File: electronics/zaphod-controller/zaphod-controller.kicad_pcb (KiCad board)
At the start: 4 copper layers, 199.9 x 69.3 mm, 220 parts, among them P1 MOLEX_43160-0102, P10 CONN_01X01, P11 MOLEX_MINIFIT_JR_2x4_WAY, P12 MOLEX_MINIFIT_JR_2x4_WAY, P13 MOLEX_MINIFIT_JR_2x4_WAY, P14 MOLEX_MINIFIT_JR_2x4_WAY, P17 CONN_01X02, P18 CONN_01X02, P19 CONN_01X02, P2 MOLEX_MINIFIT_JR_2x2_WAY, P20 CONN_01X06, P22 CONN_01X02, P23 MOLEX_KK2.54_1x4_WAY_FAN, P3 MOLEX_MINIFIT_JR_2x2_WAY, P4 MOLEX_MINIFIT_JR_2x2_WAY, P5 MOLEX_MINIFIT_JR_2x2_WAY, Q1 Si7852DP, Q2 Si7852DP, Q3 2N7002P, Q4 NTR1P02T1G, Q5 BC847B, Q6 2N7002P, SW1 B3U-1000P_SPST-NO_SMD, SW2 B3U-1000P_SPST-NO_SMD, SW3 B3U-1000P_SPST-NO_SMD, U1 ISL85410FRZ, U10 ULN2003A, U11 ULN2003A, U2 LM5116, U3 ISL85410FRZ, U4 STM32F429VET6, U5 USBLC6, U6 ACS711KEXLT_15AB, U7 ACS711KEXLT_15AB, U8 ACS711KEXLT_15AB, U9 ACS711KEXLT_15AB, X1 CSTCE8M00G55Z, X2 SWD_SMT_SOCKET, X3 ABS06-107-32.768KHZ

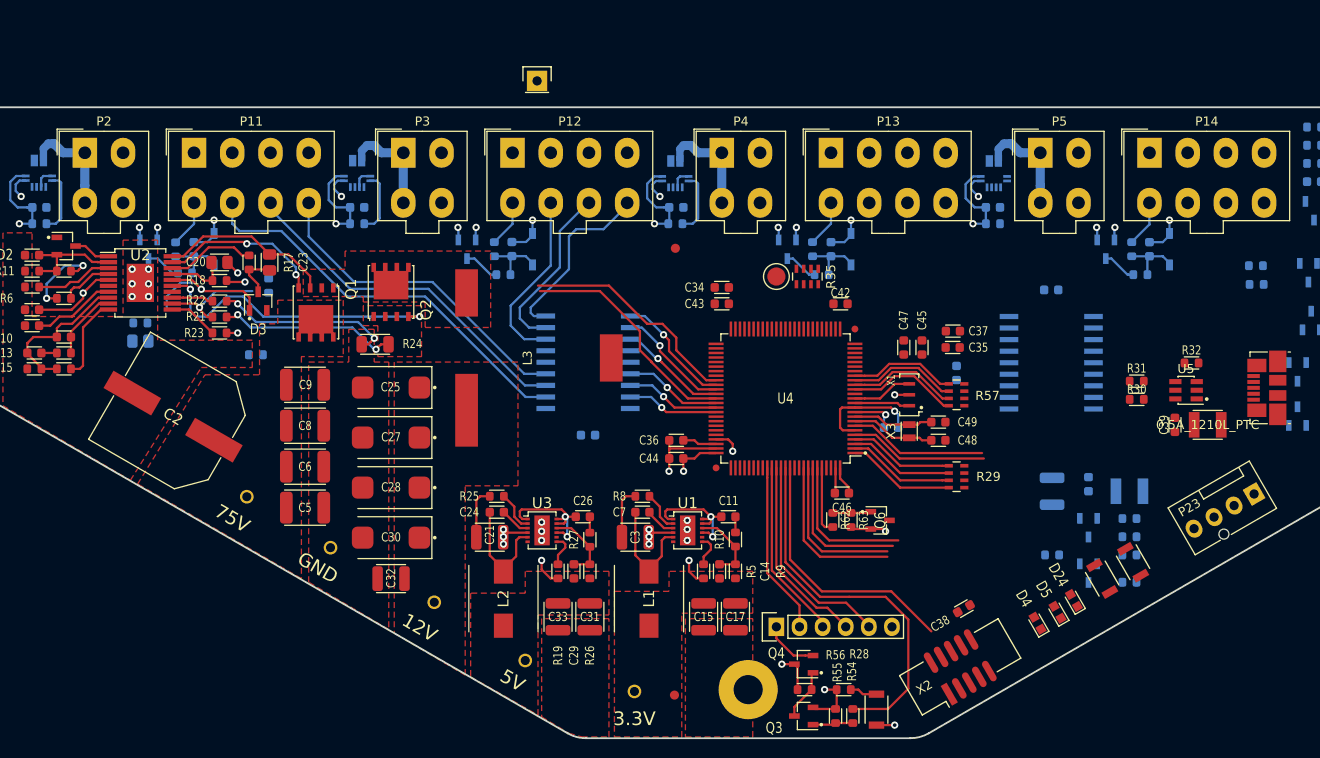
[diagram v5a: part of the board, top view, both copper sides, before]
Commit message: Continued routing and tweaks.
Updated inductor position, repinned ADC for nicer routing, most micro lines fanned out, added logo
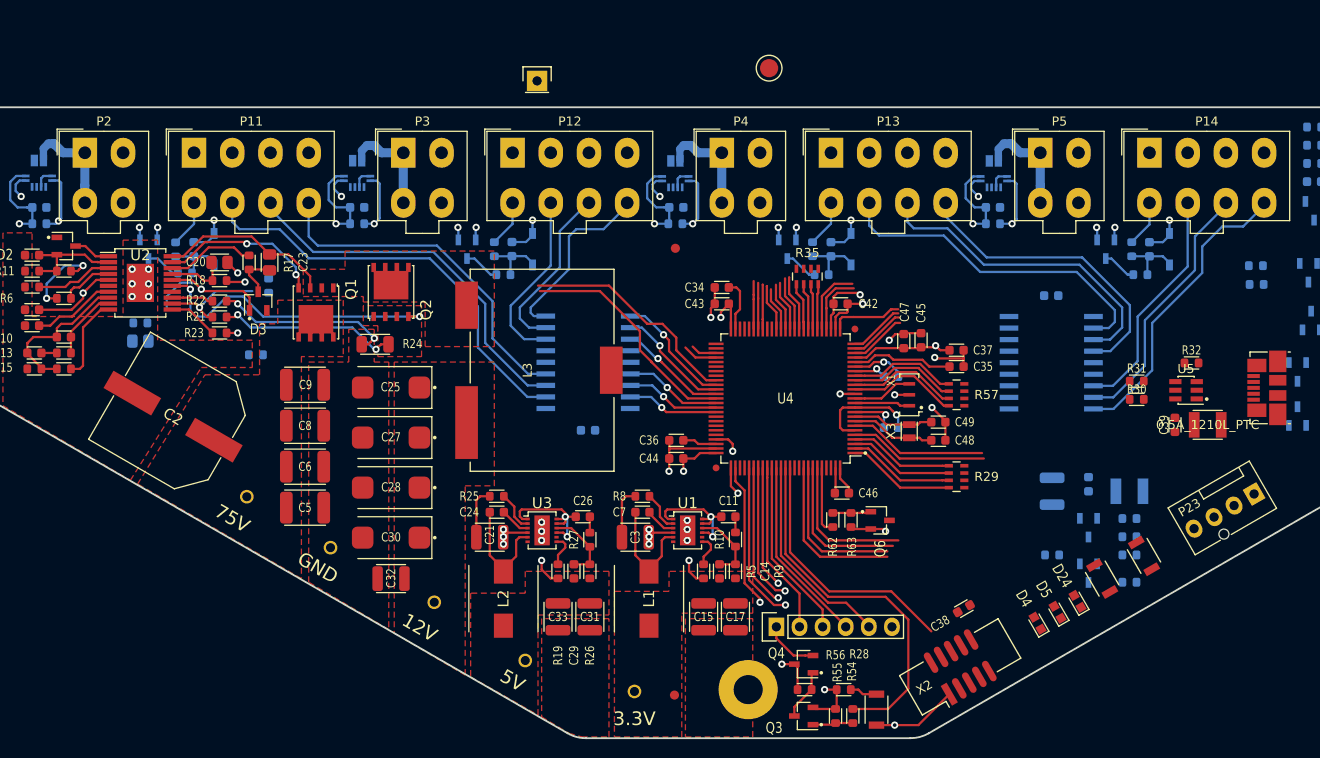
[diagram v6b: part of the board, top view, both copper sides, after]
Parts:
- added G***: LOGO, Applidyne_Logo:PANIC_LOGO890X810, F.Cu at (181.6, 98.5)
- moved TEST8 22.9 mm to (160.2, 45.7)
- moved C41 7.21 mm to (173.6, 79.6), turned to 0 degrees
- moved C35 2.14 mm to (180.8, 78.5)
- moved C37 2.14 mm to (180.8, 76.7)
- moved SW2 1.39 mm to (201.4, 99.3)
- moved L3 1.35 mm to (133.7, 78.9)
- moved C45 0.81 mm to (176.9, 75.6), turned to 90 degrees
- moved C47 0.70 mm to (175.0, 75.7), turned to 90 degrees
- moved C55 0.63 mm to (191.2, 70.7)
- moved C54 0.53 mm to (140.3, 85.5)
- moved D24 0.41 mm to (194.1, 104.3)
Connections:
- R35 pad 5: MOTOR_4_CURRENT -> MOTOR_1_CURRENT
- R35 pad 6: MOTOR_3_CURRENT -> MOTOR_2_CURRENT
- R35 pad 7: MOTOR_2_CURRENT -> MOTOR_3_CURRENT
- R35 pad 8: MOTOR_1_CURRENT -> MOTOR_4_CURRENT
- U4 pad 31: MOTOR_3_CURRENT -> MOTOR_4_CURRENT
- U4 pad 32: MOTOR_4_CURRENT -> MOTOR_3_CURRENT
- U4 pad 33: MOTOR_1_CURRENT -> MOTOR_2_CURRENT
- U4 pad 34: MOTOR_2_CURRENT -> MOTOR_1_CURRENT
- U4 pad 38: ~MOTOR_1_OC -> ~MOTOR_2_OC
- U4 pad 39: ~MOTOR_2_OC -> ~MOTOR_1_OC
- U6 pad 11: Net-(R35-Pad1) -> Net-(R35-Pad4)
- U7 pad 11: Net-(R35-Pad2) -> Net-(R35-Pad3)
- U8 pad 11: Net-(R35-Pad3) -> Net-(R35-Pad2)
- U9 pad 11: Net-(R35-Pad4) -> Net-(R35-Pad1)
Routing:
- net +3.3V: track 71.5 -> 116.4 mm, vias 12 -> 16
- net Net-(P13-Pad6): track 0.00 -> 37.3 mm
- net Net-(P13-Pad7): track 0.00 -> 35.5 mm
- net Net-(P13-Pad8): track 0.00 -> 33.6 mm
- net Net-(P14-Pad8): track 0.00 -> 33.1 mm
- net GND: track 94.6 -> 124.8 mm, vias 29 -> 35
- net Net-(P14-Pad7): track 0.00 -> 28.7 mm
- net Net-(P14-Pad6): track 0.00 -> 25.7 mm
- net EXT_OUTPUT_0: track 0.00 -> 17.5 mm, vias 0 -> 1
- net AUX_PWM_0: track 0.00 -> 15.9 mm, vias 0 -> 1
- net EXT_INPUT_1: track 0.00 -> 15.6 mm, vias 0 -> 1
- net EXT_OUTPUT_1: track 0.00 -> 15.4 mm, vias 0 -> 1
- net EXT_INPUT_0: track 0.00 -> 13.4 mm, vias 0 -> 1
- net ~MOTOR_4_OC: track 0.00 -> 13.2 mm, vias 0 -> 1
- net SERVO4_B: track 0.00 -> 7.93 mm
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
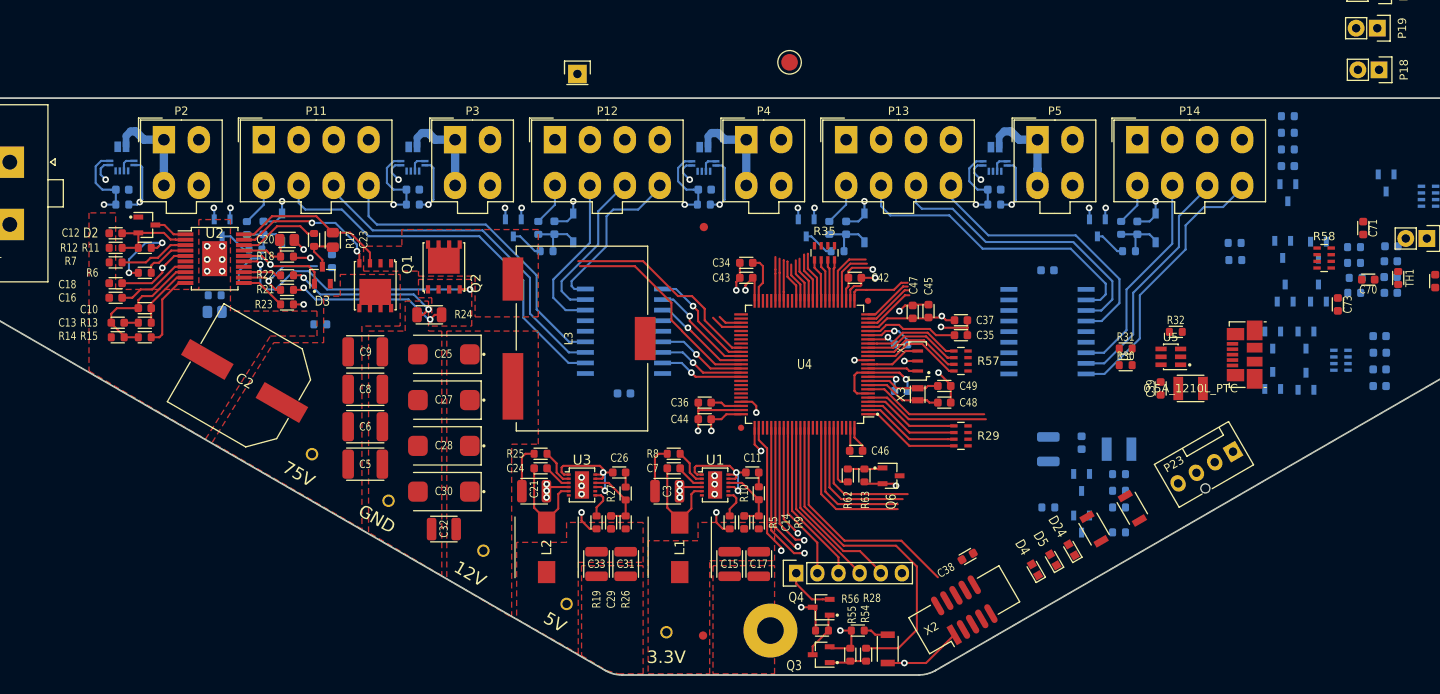
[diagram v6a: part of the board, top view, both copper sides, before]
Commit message: Minor repinning, routing, updated connector metadata
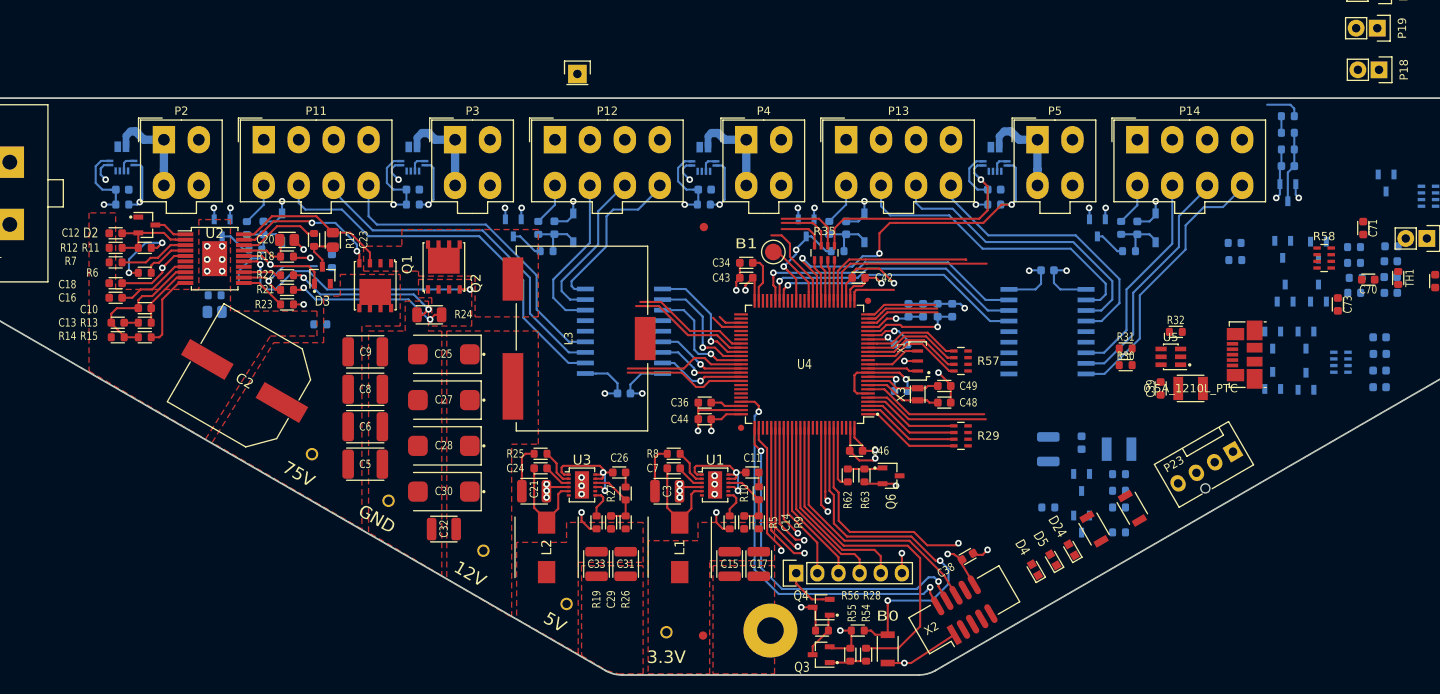
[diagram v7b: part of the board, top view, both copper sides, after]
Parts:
- removed G***: LOGO, Applidyne_Logo:PANIC_LOGO890X810
- C35, C37, C45, C47: moved to B.Cu
- moved TEST8 22.9 mm to (158.2, 68.5)
- moved C35 4.10 mm to (178.0, 75.5), turned to 90 degrees
- moved C45 2.40 mm to (174.5, 75.5)
- moved C37 1.59 mm to (179.8, 75.5), turned to 90 degrees
- moved C47 1.27 mm to (176.2, 75.5)
- moved C42 0.45 mm to (168.5, 71.6)
- moved R48 0.24 mm to (226.5, 81.8)
- moved C60 0.14 mm to (231.1, 78.8)
- moved C61 0.14 mm to (231.1, 80.8)
- moved C62 0.14 mm to (231.1, 82.8)
- moved C63 0.14 mm to (231.1, 84.8)
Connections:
- U4 pad 38: ~MOTOR_2_OC -> Net-(U4-Pad38)
- U4 pad 39: ~MOTOR_1_OC -> Net-(U4-Pad39)
- U4 pad 58: Net-(U4-Pad58) -> ~MOTOR_2_OC
- U4 pad 67: Net-(U4-Pad67) -> ~MOTOR_1_OC
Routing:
- net SWDIO: track 2.84 -> 47.4 mm, vias 1 -> 2
- net SWCLK: track 3.10 -> 42.9 mm, vias 1 -> 2
- net ~MOTOR_4_OC: track 13.2 -> 43.0 mm, vias 1 -> 3
- net SERVO3_B: track 5.27 -> 34.2 mm, vias 0 -> 1
- net SERVO3_A: track 5.07 -> 32.6 mm, vias 0 -> 1
- net GND: track 124.8 -> 152.1 mm, vias 35 -> 40
- net SERVO3_EN: track 4.87 -> 31.5 mm, vias 0 -> 1
- net Net-(R35-Pad1): track 2.86 -> 28.3 mm
- net BOOT0: track 19.6 -> 44.8 mm, vias 0 -> 2
- net AUX_ANALOG_0: track 6.89 -> 21.3 mm
- net +12V: track 23.5 -> 37.8 mm, vias 9 -> 11
- net AUX_ANALOG_1: track 7.52 -> 19.6 mm
- net SERVO1_HLFB: track 29.4 -> 18.3 mm
- net FAN_PWM: track 16.1 -> 27.1 mm, vias 0 -> 1
- net SERVO2_HLFB: track 28.6 -> 18.7 mm
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- added copper zone on In2.Cu, net +3.3V
- added copper zone on In1.Cu, net GND
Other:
- board text added: "B0"
- board text added: "B1"

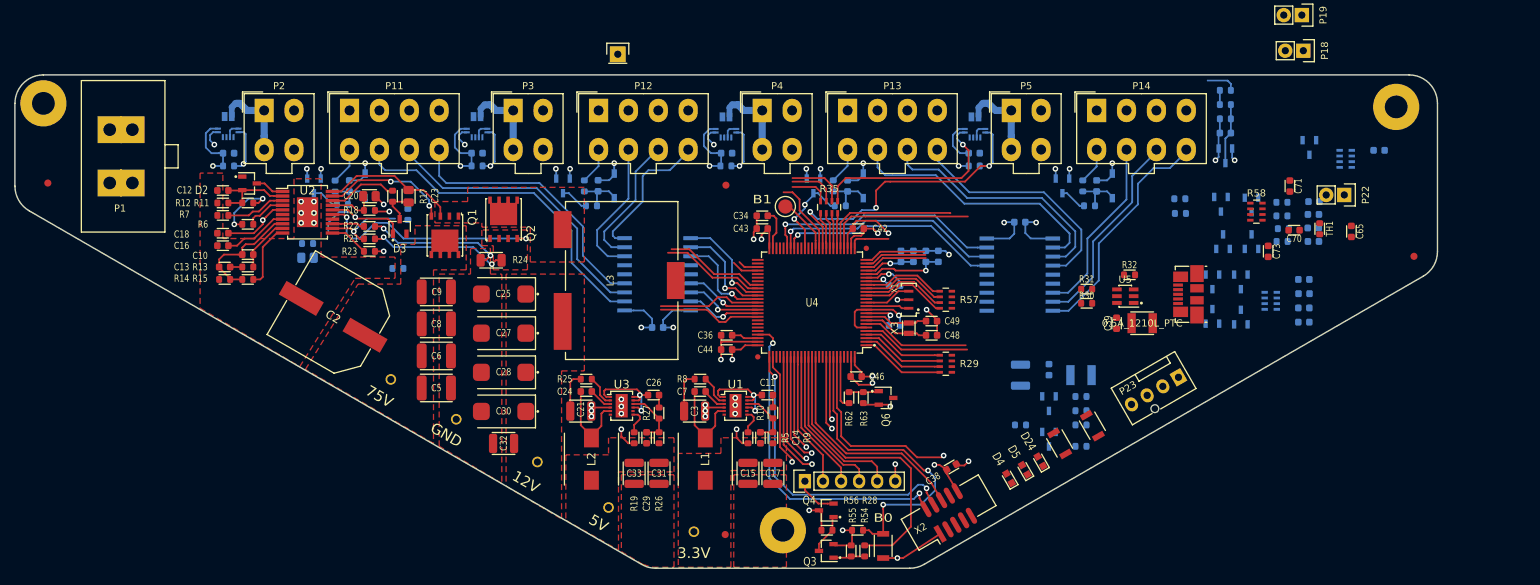
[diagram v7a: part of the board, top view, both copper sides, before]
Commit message: Routing, connector changes, repinning/resistor changes
Misc other cleanup and improvements while routing
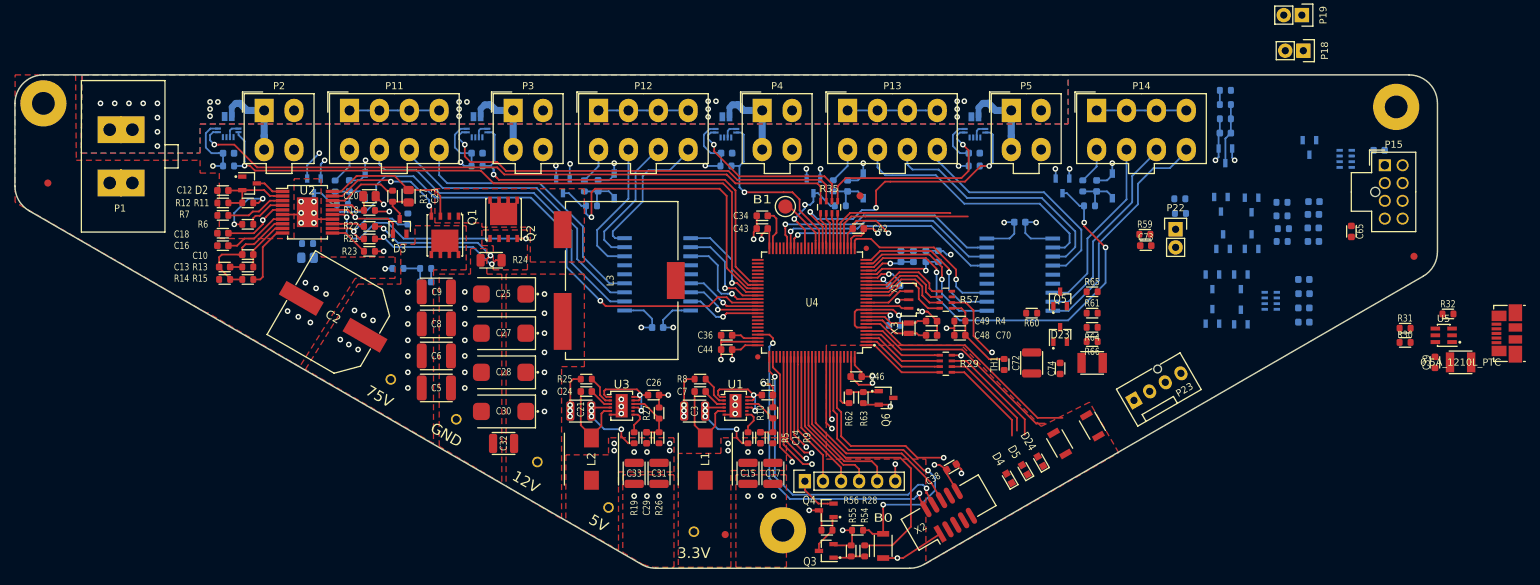
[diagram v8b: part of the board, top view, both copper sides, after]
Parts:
- removed MNT5: MNT_M3_PLATED, Applidyne_Mount:MTGP650H330
- removed P10: CONN_01X01, Applidyne_Connector_Wurth:61300111121
- added LOGO1: LOGO, Applidyne_Logo:PANIC_LOGO890X810, F.Cu at (182.3, 98.5)
- added MNT2: MNT_M3_PLATED, Applidyne_Mount:MTGP650H330, F.Cu at (157.9, 114.0)
- added P15: MOLEX_NANOFIT_2x4_WAY, Applidyne_Connector_Molex:Molex_Nano-Fit_105310-xx08_2x04_VERT, F.Cu at (242.5, 62.7)
- added R4: 10K0_1608M, Applidyne_Resistor:RESC1608X50N, F.Cu at (182.8, 84.6)
- added R59: 10K0_1608M, Applidyne_Resistor:RESC1608X50N, F.Cu at (208.8, 72.4)
- C71: moved to B.Cu
- C72, C74, D23, F2, Q5, R60, R61, R64, R65, R66: moved to F.Cu
- R58: value 10K_QUAD_ARRAY_1608M -> 10K0_1608M; footprint Applidyne_Resistor:R_Array_Concave_4x1608M -> Applidyne_Resistor:RESC1608X50N; moved to B.Cu
- moved C71 122.2 mm to (107.7, 79.1), turned to 180 degrees
- moved R58 117.0 mm to (107.7, 77.2)
- moved C70 49.2 mm to (182.8, 86.6), turned to 0 degrees
- moved TH1 48.3 mm to (189.0, 90.7), turned to 90 degrees
- moved C39 45.1 mm to (249.6, 90.4)
- moved F1 45.1 mm to (253.2, 90.4)
- moved R30 45.1 mm to (245.3, 87.6)
- moved R31 45.1 mm to (245.3, 85.6)
- moved R32 45.1 mm to (251.4, 83.6)
- moved U5 45.1 mm to (250.8, 86.6)
- moved J?1 45.1 mm to (259.5, 86.3)
- moved P22 24.2 mm to (213.1, 71.7), turned to 0 degrees
- moved R65 21.8 mm to (201.4, 80.5)
- moved Q5 19.8 mm to (196.9, 81.5)
- moved FID3 18.9 mm to (168.8, 67.0)
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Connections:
- R58 pad 1: Net-(C70-Pad2) -> Net-(C71-Pad2)
- R58 pad 2: Net-(C71-Pad2) -> GND
- U4 pad 57: Net-(U4-Pad57) -> ~MOTOR_2_OC
- U4 pad 58: ~MOTOR_2_OC -> ~MOTOR_1_OC
- U4 pad 67: ~MOTOR_1_OC -> Net-(U4-Pad67)
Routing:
- net Net-(R35-Pad4): track 8.39 -> 92.5 mm
- net ~MOTOR_1_OC: track 21.5 -> 91.9 mm
- net +12V: track 37.8 -> 98.3 mm, vias 11 -> 18
- net SERVO1_HLFB: track 18.3 -> 78.4 mm, vias 0 -> 1
- net Net-(R35-Pad3): track 9.82 -> 59.3 mm
- net SERVO4_HLFB: track 12.6 -> 58.1 mm, vias 0 -> 3
- net ~MOTOR_2_OC: track 21.1 -> 57.9 mm
- net SERVO2_HLFB: track 18.7 -> 44.8 mm, vias 0 -> 1
- net GND: track 152.1 -> 173.8 mm, vias 40 -> 68
- net SERVO4_B: track 5.93 -> 24.3 mm, vias 0 -> 1
- net BUTTON_0: track 15.2 -> 33.0 mm
- net Net-(D24-PadA): track 0.00 -> 15.8 mm
- net BUTTON_1: track 15.2 -> 30.5 mm
- net Net-(C71-Pad2): track 0.00 -> 14.9 mm, vias 0 -> 1
- net SERVO4_EN: track 8.82 -> 22.9 mm, vias 0 -> 1
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- added copper zone on B.Cu, net +POWER
